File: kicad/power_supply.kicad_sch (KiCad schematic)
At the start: 56 parts, among them J2 Conn_01x01_Female, J3 Conn_01x01_Female, Q1 2N2905A, Q2 2N2905A, Q3 2N3904, Q4 2N3904, T1 Transformer_1P_2S, U11 7406, U18 LM7805_TO220, U19 LM317SP_TO220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

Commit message: KiCAD: Adjust courtyards
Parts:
- C11, C6: footprint Capacitor_THT:CP_Radial_Tantal_D4.5mm_P5.00mm -> custom_footprints:CP_Radial_Tantal_D4.5mm_P5.00mm
- Q1, Q2: footprint Package_TO_SOT_THT:TO-39-3 -> custom_footprints:TO-39-3
- RV1, RV2, RV3: footprint Potentiometer_THT:Potentiometer_Bourns_3339P_Vertical -> custom_footprints:Potentiometer_Bourns_3339P_Vertical_HandSoldering
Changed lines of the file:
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@@
     (property "Reference" "RV3" (id 0) (at 135.89 41.91 90))
     (property "Value" "1K0" (id 1) (at 135.89 44.45 90))
-    (property "Footprint" "Potentiometer_THT:Potentiometer_Bourns_3339P_Vertical" (id 2) (at 142.24 45.72 0)
+    (property "Footprint" "custom_footprints:Potentiometer_Bourns_3339P_Vertical_HandSoldering" (id 2) (at 142.24 45.72 0)
       (effects (font (size 1.27 1.27)) hide)
     )
@@
     (property "Reference" "RV1" (id 0) (at 157.48 72.39 0))
     (property "Value" "1K0" (id 1) (at 157.48 74.93 0))
-    (property "Footprint" "Potentiometer_THT:Potentiometer_Bourns_3339P_Vertical" (id 2) (at 161.29 73.66 0)
+    (property "Footprint" "custom_footprints:Potentiometer_Bourns_3339P_Vertical_HandSoldering" (id 2) (at 161.29 73.66 0)
       (effects (font (size 1.27 1.27)) hide)
     )
@@
       (effects (font (size 1.27 1.27)) (justify left))
     )
-    (property "Footprint" "Capacitor_THT:CP_Radial_Tantal_D4.5mm_P5.00mm" (id 2) (at 209.2452 138.43 0)
+    (property "Footprint" "custom_footprints:CP_Radial_Tantal_D4.5mm_P5.00mm" (id 2) (at 209.2452 138.43 0)
       (effects (font (size 1.27 1.27)) hide)
     )
@@
       (effects (font (size 1.27 1.27)) (justify left))
     )
-    (property "Footprint" "Capacitor_THT:CP_Radial_Tantal_D4.5mm_P5.00mm" (id 2) (at 181.3052 69.85 0)
+    (property "Footprint" "custom_footprints:CP_Radial_Tantal_D4.5mm_P5.00mm" (id 2) (at 181.3052 69.85 0)
       (effects (font (size 1.27 1.27)) hide)
     )
@@
     (property "Reference" "Q1" (id 0) (at 232.41 107.95 90))
     (property "Value" "2N2905A" (id 1) (at 232.41 110.49 90))
-    (property "Footprint" "Package_TO_SOT_THT:TO-39-3" (id 2) (at 230.505 111.76 0)
+    (property "Footprint" "custom_footprints:TO-39-3" (id 2) (at 230.505 111.76 0)
       (effects (font (size 1.27 1.27) italic) (justify left) hide)
     )
@@
     (property "Reference" "RV2" (id 0) (at 147.32 49.53 90))
     (property "Value" "5K0" (id 1) (at 147.32 52.07 90))
-    (property "Footprint" "Potentiometer_THT:Potentiometer_Bourns_3339P_Vertical" (id 2) (at 142.24 54.61 0)
+    (property "Footprint" "custom_footprints:Potentiometer_Bourns_3339P_Vertical_HandSoldering" (id 2) (at 142.24 54.61 0)
       (effects (font (size 1.27 1.27)) hide)
     )
@@
     (property "Reference" "Q2" (id 0) (at 231.14 22.86 90))
     (property "Value" "2N2905A" (id 1) (at 231.14 25.4 90))
-    (property "Footprint" "Package_TO_SOT_THT:TO-39-3" (id 2) (at 229.235 26.67 0)
+    (property "Footprint" "custom_footprints:TO-39-3" (id 2) (at 229.235 26.67 0)
       (effects (font (size 1.27 1.27) italic) (justify left) hide)
     )

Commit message: KiCAD: Added R19 (VCCEnable pullup)
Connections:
- net AC2: now reaches D4.2, T1.4 (SB)
- net AC1: now reaches D4.4, T1.3 (SA)
- net AC4: now reaches C9.2, T1.6 (SD)
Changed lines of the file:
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@@
+    (effects (font (size 1.27 1.27)) (justify left bottom))
+  )
+  (label "AC2" (at 74.93 119.38 0)
     (effects (font (size 1.27 1.27)) (justify left bottom))
   )
   (label "28VDC" (at 113.03 29.21 0)
+    (effects (font (size 1.27 1.27)) (justify left bottom))
+  )
+  (label "AC4" (at 74.93 106.68 0)
+    (effects (font (size 1.27 1.27)) (justify left bottom))
+  )
+  (label "AC1" (at 74.93 134.62 0)
     (effects (font (size 1.27 1.27)) (justify left bottom))
   )
@@
     (pin "7")
   )
-  (symbol (lib_id "power:GND") (at 255.27 92.71 0) (unit 1)
-    (in_bom yes) (on_board yes) (fields_autoplaced)
-    (property "Reference" "#PWR0148" (id 0) (at 255.27 99.06 0)
-      (effects (font (size 1.27 1.27)) hide)
-    )
-    (property "Value" "GND" (id 1) (at 255.27 97.79 0))
-    (property "Footprint" "" (id 2) (at 255.27 92.71 0)
-      (effects (font (size 1.27 1.27)) hide)
-    )
-    (property "Datasheet" "" (id 3) (at 255.27 92.71 0)
-      (effects (font (size 1.27 1.27)) hide)
-    )
-    (pin "1")
-  )
   (symbol (lib_id "Mechanical:MountingHole") (at 25.4 165.1 0) (unit 1)

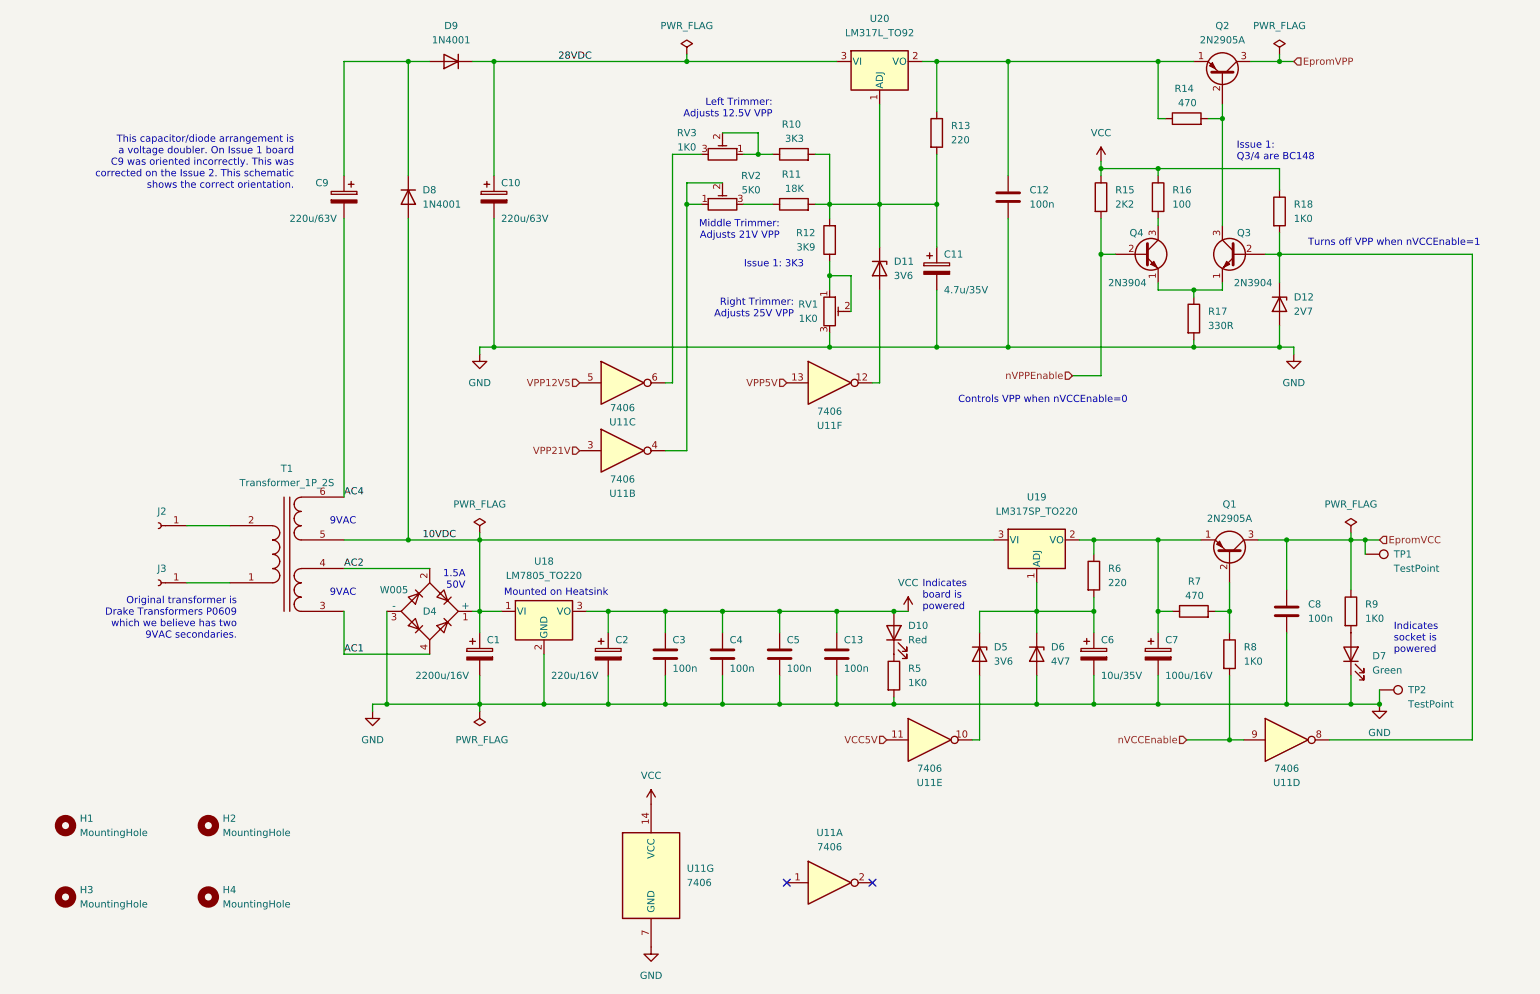
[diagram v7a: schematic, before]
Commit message: KiCAD: Replace transformer with DC Jack + Boost Converter
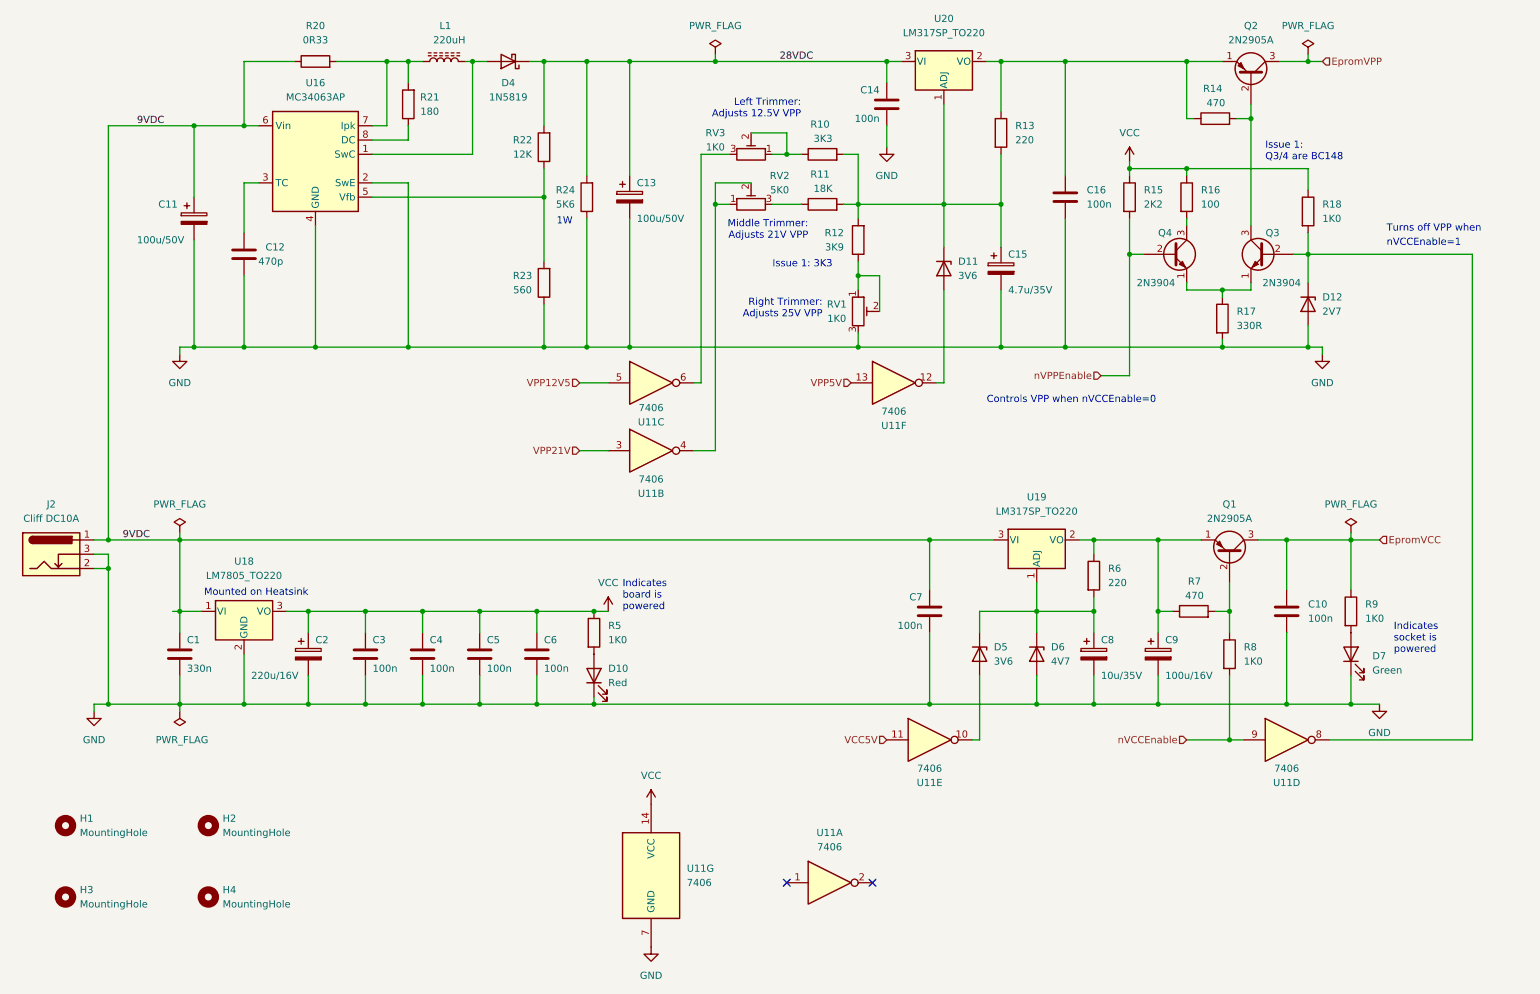
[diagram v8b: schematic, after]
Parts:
- removed C1: 2200u/16V, Capacitor_THT:CP_Radial_D13.0mm_P5.00mm, symbol Device:C_Polarized
- removed C9: 220u/63V, Capacitor_THT:CP_Radial_D10.0mm_P5.00mm, symbol Device:C_Polarized
- removed D4: W005, Diode_THT:Diode_Bridge_Round_D9.0mm, symbol Diode_Bridge:W005G
- removed D8, D9: 1N4001, custom_footprints:D_DO-41_SOD81_P11.43mm_Horizontal, symbol Diode:1N4001
- removed J2, J3: Conn_01x01_Female, TestPoint:TestPoint_THTPad_D3.0mm_Drill1.5mm, symbol Connector:Conn_01x01_Female
- removed T1: Transformer_1P_2S, custom_footprints:Transformer_drake_p0609, symbol Device:Transformer_1P_2S
- removed TP1, TP2: TestPoint, TestPoint:TestPoint_THTPad_D1.5mm_Drill0.7mm, symbol Connector:TestPoint
- removed U20: LM317L_TO92, Package_TO_SOT_THT:TO-92_Inline_Wide, symbol Regulator_Linear:LM317L_TO92
- added C1: 330n, Capacitor_THT:C_Disc_D4.3mm_W1.9mm_P5.00mm, symbol Device:C
- added C11: 100u/50V, Capacitor_THT:CP_Radial_D8.0mm_P5.00mm, symbol Device:C_Polarized
- added C12: 470p, Capacitor_THT:C_Disc_D4.3mm_W1.9mm_P5.00mm, symbol Device:C
- added C14, C7: 100n, Capacitor_THT:C_Disc_D4.3mm_W1.9mm_P5.00mm, symbol Device:C
- added D4: 1N5819, Diode_THT:D_DO-41_SOD81_P10.16mm_Horizontal, symbol Diode:1N5819
- added J2: Cliff DC10A, custom_footprints:CLIFF_FC68148(DC-10A), symbol Connector:Barrel_Jack_Switch
- added L1: 220uH, Inductor_THT:L_Radial_D14.2mm_P10.00mm_Neosid_SD14, symbol Device:L_Ferrite
- added R20: 0R33, custom_footprints:R_Axial_DIN0207_L6.3mm_D2.0mm_P10.16mm_Horizontal, symbol Device:R
- added R21: 180, custom_footprints:R_Axial_DIN0207_L6.3mm_D2.0mm_P10.16mm_Horizontal, symbol Device:R
- added R22: 12K, custom_footprints:R_Axial_DIN0207_L6.3mm_D2.0mm_P10.16mm_Horizontal, symbol Device:R
- added R23: 560, custom_footprints:R_Axial_DIN0207_L6.3mm_D2.0mm_P10.16mm_Horizontal, symbol Device:R
- added R24: 5K6, Resistor_THT:R_Axial_DIN0207_L6.3mm_D2.5mm_P10.16mm_Horizontal, symbol Device:R
- added U16: MC34063AP, Package_DIP:DIP-8_W7.62mm, symbol Regulator_Switching:MC34063AP
- added U20: LM317SP_TO220, Package_TO_SOT_THT:TO-220-3_Vertical, symbol Regulator_Linear:LM317_TO-220
- C13: renamed from C10; value 220u/63V -> 100u/50V; footprint Capacitor_THT:CP_Radial_D10.0mm_P5.00mm -> Capacitor_THT:CP_Radial_D8.0mm_P5.00mm
- R5: footprint custom_footprints:R_Axial_DIN0207_L6.3mm_D2.0mm_P11.43mm_Horizontal -> custom_footprints:R_Axial_DIN0207_L6.3mm_D2.0mm_P10.16mm_Horizontal
- renumbered C8 to C10, C11 to C15, C12 to C16, C13 to C6, C6 to C8, C7 to C9
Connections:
- net 28VDC: now also C14.1, D4.1 (K), R22.2, R24.2, U20.3 (VI)
- net GND: now also D10.1 (K), C1.2, C11.2, C12.2, C14.2, C7.2, J2.2, J2.3, R23.1, R24.1, U16.2 (SwE), U16.4 (GND); no longer R5.2
- net VCC: now also R5.1; no longer D10.2 (A)
- net at C16.1, Q2.1 (E), R13.1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: now also U20.2 (VO)
- net at C15.1, D11.1 (K), R10.2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: now also U20.1 (ADJ)
- net 10VDC renamed 9VDC
- net 9VDC: now also C1.1, C11.1, C7.1, J2.1, R20.1, U16.6 (Vin)
- new net: D10.2 (A), R5.2
- new net: D4.2 (A), L1.2, U16.1 (SwC)
- new net: L1.1, R20.2, R21.2, U16.7 (Ipk)
- new net: R21.1, U16.8 (DC)
- new net: C12.1, U16.3 (TC)
- new net: R22.1, R23.2, U16.5 (Vfb)
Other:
- note added: "1W"
- note added: "Turns off VPP when"
- note added: "nVCCEnable=1"
- note removed: "1.5A 50V"
- note removed: "9VAC"
- note removed: "Original transformer is Drake Transformers P0609 which we believe has two 9VAC secondaries."
- note removed: "This capacitor/diode arrangement is a voltage doubler. On Issue 1 board C9 was oriented incorrectly. This was corrected on the Issue 2. This schematic shows the correct orientation."
- note removed: "Turns off VPP when nVCCEnable=1"
- moved on the sheet: C13, C15, C16, C2, C3, C4, C5, C6, D10, D11, D12, Q2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
